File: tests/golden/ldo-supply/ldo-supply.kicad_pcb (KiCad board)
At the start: 2 copper layers, 40 x 36 mm, 7 parts, among them J1 CONN_PWR_1X02, J2 CONN_PWR_1X02, U1 AMS1117_3V3

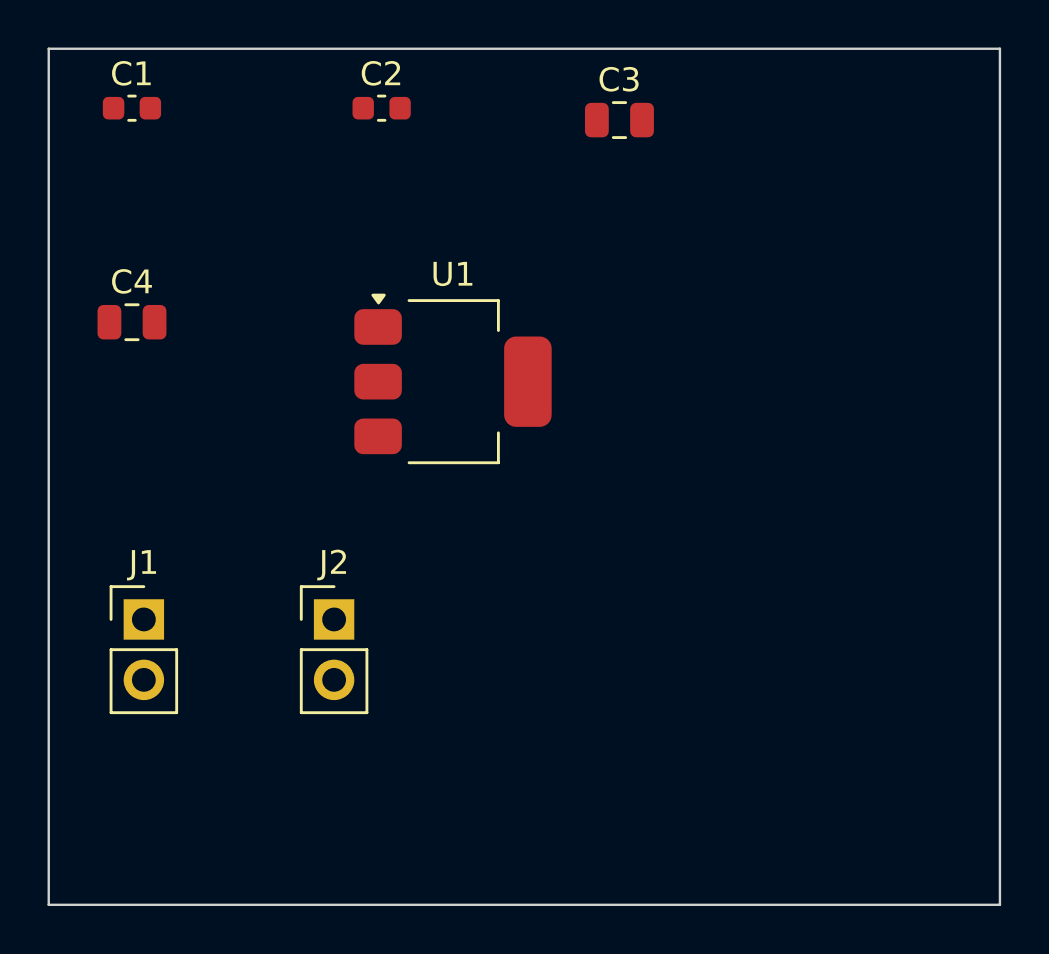
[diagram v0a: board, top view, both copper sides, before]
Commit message: M7a+M7b: topological routing — sketches in source, DRC-clean copper out
Routes are stored as topology: which obstacles a wire passes and on which side.
Nothing in the source is a coordinate, so moving a part leaves the sketch true and
only the tightening re-runs — which is the whole point of the approach (ADR 0006,
written after reading SURF, Maley, TopoR and the shortest-homotopic-path
literature).

Geometry comes from the classical pipeline: inflate obstacles by the clearance the
net needs, triangulate what is left (constrained Delaunay, via Shapely/GEOS), turn
the sketch into a crossing sequence, reduce it to a canonical homotopy class, and
tighten the resulting sleeve with the funnel algorithm. Inflating first is what
makes the shortest path automatically a legal one.

All four examples route with **zero DRC violations and zero schematic-parity
issues**; ldo-supply routes completely, 13 of 13 connections with nothing
unconnected. Unroutable connections are reported with a reason.

Almost every defect here was invisible to structural checks — the sleeve stayed
valid, the funnel still terminated, and the board was still legal. Each was found by
measuring the result:

* portal orientation had the wrong sign for Y-down board coordinates, turning a
  24.6 mm route into a 162.6 mm zigzag between the pad rows.
* searching triangle centroids instead of portal midpoints sent routes to the board
  corner and back, because a CDT of sparse obstacles has a few enormous triangles.
* an A* node has to be a *crossing*, not a diagonal: keyed on the diagonal alone the
  search steps through one without crossing it.
* feeding a finished route back as one convex hull swallowed the area inside every
  bend, costing a third of the connections.
* track obstacles pre-inflated by the routed net's own half-width left every later
  track short by half of its own, exactly as DRC reported.
* KiCad enforces the larger of two nets' clearances, not the routing net's.
* four shield tabs sharing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
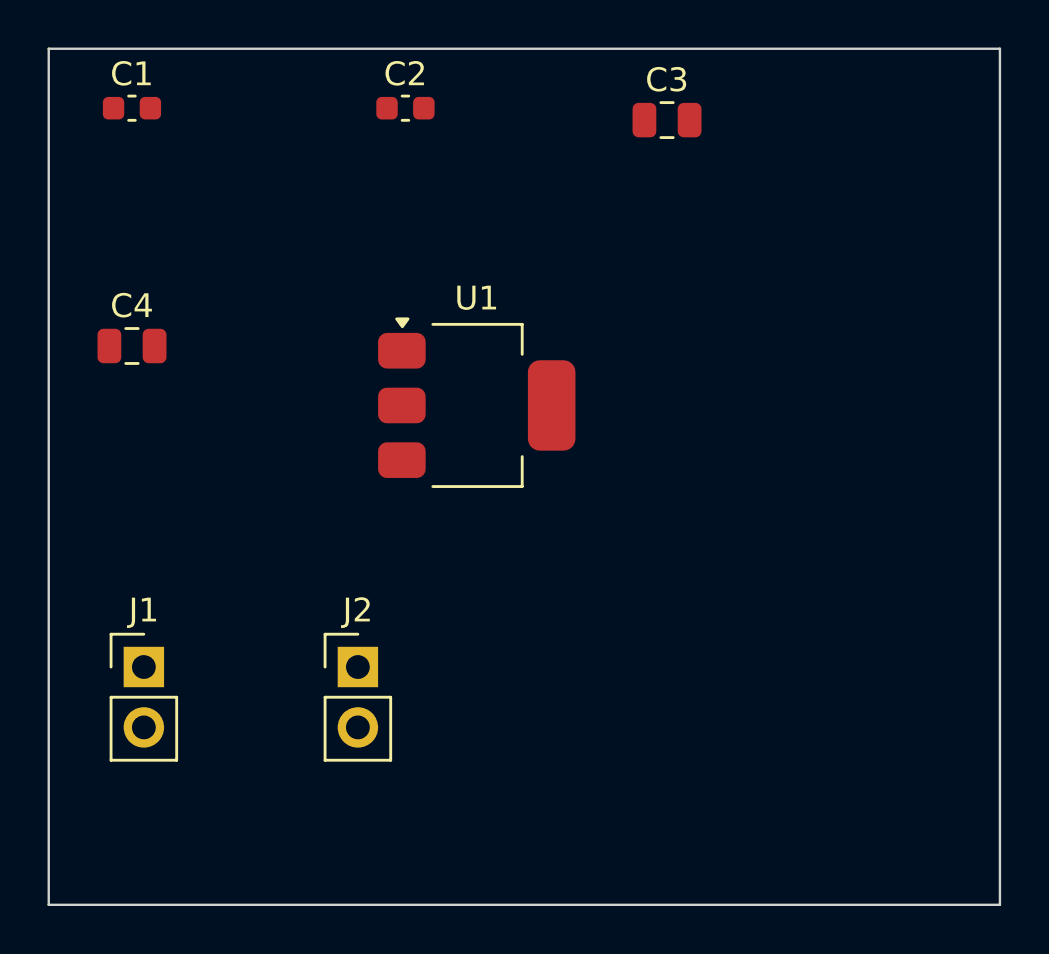
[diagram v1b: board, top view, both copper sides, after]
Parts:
- moved J2 2.24 mm to (113.0, 126.0)
- moved C3 2.00 mm to (126.0, 103.0)
- moved J1 2.00 mm to (104.0, 126.0)
- moved U1 1.41 mm to (118.0, 115.0)
- moved C2 1.00 mm to (115.0, 102.5)
- moved C4 1.00 mm to (103.5, 112.5)
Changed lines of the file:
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@@
 	(footprint "Capacitor_SMD:C_0603_1608Metric"
 		(layer "F.Cu")
-		(at 114 102.5 0)
+		(at 115 102.5 0)
 		(descr "Capacitor SMD 0603 (1608 Metric), square (rectangular) end terminal, IPC-7351 nominal, (Body size source: IPC-SM-782 page 76, https://www.pcb-3d.com/wordpress/wp-content/uploads/ipc-sm-782a_amendment_1_and_2.pdf), generated with kicad-footprint-generator")
 		(tags "capacitor")
@@
 	(footprint "Capacitor_SMD:C_0805_2012Metric"
 		(layer "F.Cu")
-		(at 124 103 0)
+		(at 126 103 0)
 		(descr "Capacitor SMD 0805 (2012 Metric), square (rectangular) end terminal, IPC-7351 nominal, (Body size source: IPC-SM-782 page 76, https://www.pcb-3d.com/wordpress/wp-content/uploads/ipc-sm-782a_amendment_1_and_2.pdf, https://docs.google.com/spreadsheets/d/1BsfQQcO9C6DZCsRaXUlFlo91Tg2WpOkGARC1WS5S8t0/edit?usp=sharing), generated with kicad-footprint-generator")
 		(tags "capacitor")
@@
 	(footprint "Capacitor_SMD:C_0805_2012Metric"
 		(layer "F.Cu")
-		(at 103.5 111.5 0)
+		(at 103.5 112.5 0)
 		(descr "Capacitor SMD 0805 (2012 Metric), square (rectangular) end terminal, IPC-7351 nominal, (Body size source: IPC-SM-782 page 76, https://www.pcb-3d.com/wordpress/wp-content/uploads/ipc-sm-782a_amendment_1_and_2.pdf, https://docs.google.com/spreadsheets/d/1BsfQQcO9C6DZCsRaXUlFlo91Tg2WpOkGARC1WS5S8t0/edit?usp=sharing), generated with kicad-footprint-generator")
 		(tags "capacitor")
@@
 	(footprint "Connector_PinHeader_2.54mm:PinHeader_1x02_P2.54mm_Vertical"
 		(layer "F.Cu")
-		(at 104 124 0)
+		(at 104 126 0)
 		(descr "Through hole straight pin header, 1x02, 2.54mm pitch, single row")
 		(tags "Through hole pin header THT 1x02 2.54mm single row")
@@
 	(footprint "Connector_PinHeader_2.54mm:PinHeader_1x02_P2.54mm_Vertical"
 		(layer "F.Cu")
-		(at 112 124 0)
+		(at 113 126 0)
 		(descr "Through hole straight pin header, 1x02, 2.54mm pitch, single row")
 		(tags "Through hole pin header THT 1x02 2.54mm single row")
@@
 	(footprint "Package_TO_SOT_SMD:SOT-223-3_TabPin2"
 		(layer "F.Cu")
-		(at 117 114 0)
+		(at 118 115 0)
 		(descr "module CMS SOT223 4 pins")
 		(tags "CMS SOT")
